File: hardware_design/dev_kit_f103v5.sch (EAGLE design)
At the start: 57 parts, among them J2 CON-SD-CARD_MICROSD-2908-05, U2 FT232RLSSOP, Y1 32.768kHz

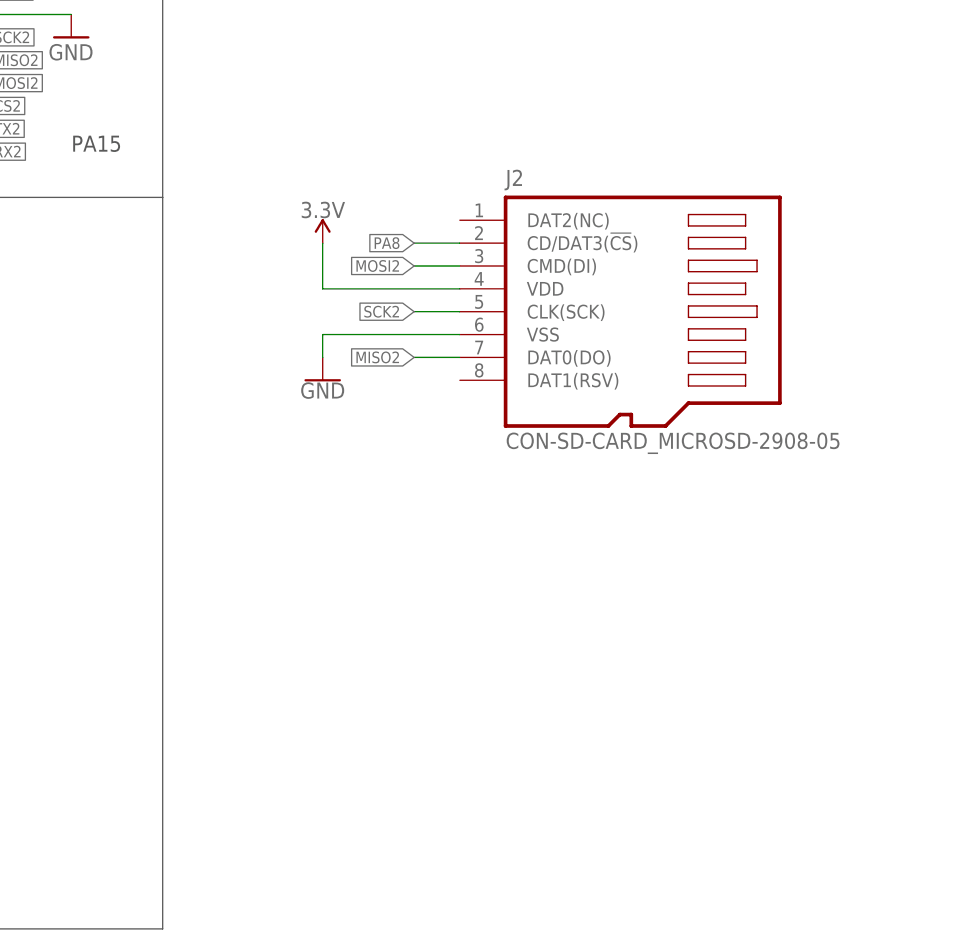
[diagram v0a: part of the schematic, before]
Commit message: Drill size was changed (20 mil)
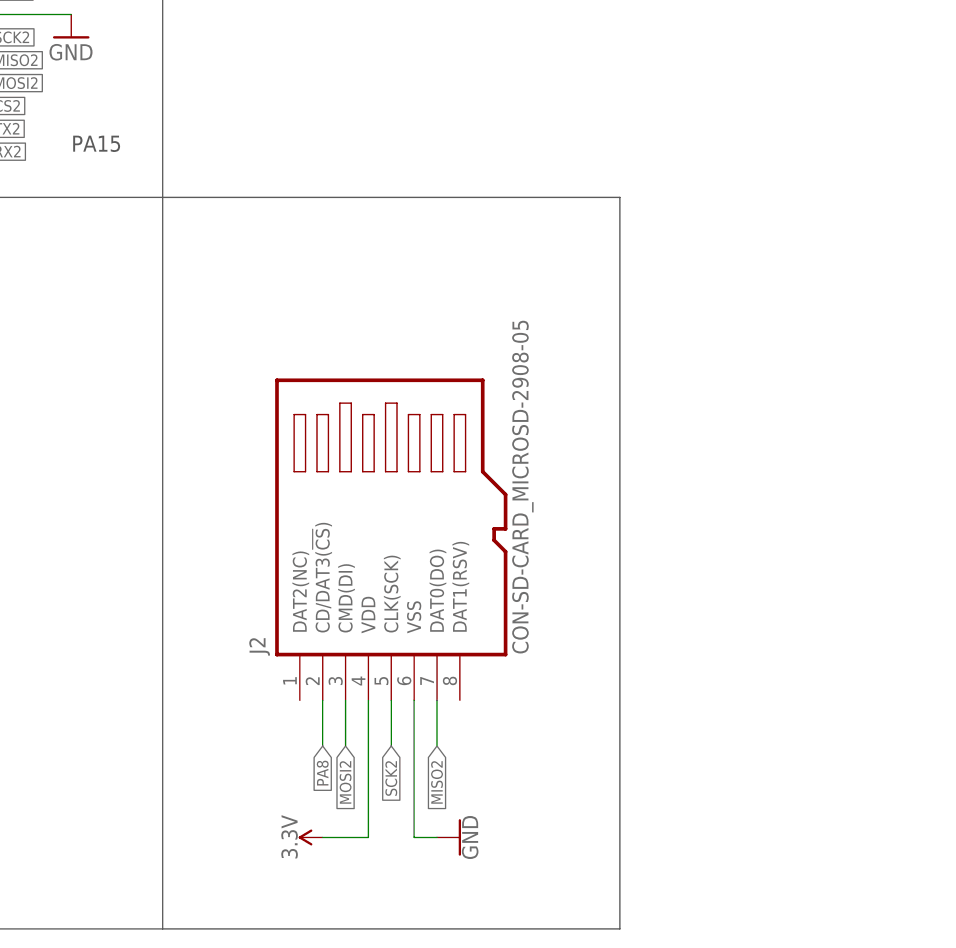
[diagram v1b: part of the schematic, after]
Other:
- moved on the sheet: J2
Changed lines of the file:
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@@
 <text x="139.7" y="139.7" size="1.778" layer="97">PB3</text>
 <text x="7.62" y="15.24" size="1.27" layer="97">CRX3, CTX3, CS2, BUTTON</text>
+<wire x1="180.34" y1="93.98" x2="231.14" y2="93.98" width="0.1524" layer="97"/>
+<wire x1="231.14" y1="93.98" x2="231.14" y2="12.7" width="0.1524" layer="97"/>
+<wire x1="231.14" y1="12.7" x2="180.34" y2="12.7" width="0.1524" layer="97"/>
 </plain>
 <instances>
@@
 <attribute name="VALUE" x="0" y="26.67" size="1.778" layer="96"/>
 </instance>
-<instance part="J2" gate="G$1" x="231.14" y="81.28" smashed="yes">
-<attribute name="NAME" x="218.44" y="95.25" size="1.778" layer="95"/>
-<attribute name="VALUE" x="218.44" y="66.04" size="1.778" layer="96"/>
-</instance>
-<instance part="SUPPLY17" gate="G$1" x="198.12" y="88.9" smashed="yes">
-<attribute name="VALUE" x="198.12" y="91.694" size="1.778" layer="96" align="bottom-center"/>
-</instance>
-<instance part="GND24" gate="1" x="198.12" y="73.66" smashed="yes">
-<attribute name="VALUE" x="198.12" y="73.406" size="1.778" layer="96" align="top-center"/>
+<instance part="J2" gate="G$1" x="205.74" y="55.88" smashed="yes" rot="R90">
+<attribute name="NAME" x="191.77" y="43.18" size="1.778" layer="95" rot="R90"/>
+<attribute name="VALUE" x="220.98" y="43.18" size="1.778" layer="96" rot="R90"/>
+</instance>
+<instance part="SUPPLY17" gate="G$1" x="198.12" y="22.86" smashed="yes" rot="R90">
+<attribute name="VALUE" x="195.326" y="22.86" size="1.778" layer="96" rot="R90" align="bottom-center"/>
+</instance>
+<instance part="GND24" gate="1" x="213.36" y="22.86" smashed="yes" rot="R90">
+<attribute name="VALUE" x="213.614" y="22.86" size="1.778" layer="96" rot="R90" align="top-center"/>
 </instance>
 <instance part="F1" gate="G$1" x="-60.96" y="137.16" smashed="yes">
@@
 <segment>
 <pinref part="J2" gate="G$1" pin="VSS"/>
-<wire x1="213.36" y1="78.74" x2="198.12" y2="78.74" width="0.1524" layer="91"/>
+<wire x1="208.28" y1="38.1" x2="208.28" y2="22.86" width="0.1524" layer="91"/>
 <pinref part="GND24" gate="1" pin="GND"/>
-<wire x1="198.12" y1="78.74" x2="198.12" y2="76.2" width="0.1524" layer="91"/>
+<wire x1="208.28" y1="22.86" x2="210.82" y2="22.86" width="0.1524" layer="91"/>
 </segment>
 </net>
@@
 <segment>
 <pinref part="SUPPLY17" gate="G$1" pin="3.3V"/>
-<wire x1="198.12" y1="88.9" x2="198.12" y2="83.82" width="0.1524" layer="91"/>
+<wire x1="198.12" y1="22.86" x2="203.2" y2="22.86" width="0.1524" layer="91"/>
 <pinref part="J2" gate="G$1" pin="VDD"/>
-<wire x1="198.12" y1="83.82" x2="213.36" y2="83.82" width="0.1524" layer="91"/>
+<wire x1="203.2" y1="22.86" x2="203.2" y2="38.1" width="0.1524" layer="91"/>
 </segment>
 </net>
@@
 <segment>
 <pinref part="J2" gate="G$1" pin="CMD(DI)"/>
-<wire x1="213.36" y1="86.36" x2="208.28" y2="86.36" width="0.1524" layer="91"/>
-<label x="208.28" y="86.36" size="1.27" layer="95" rot="R180" xref="yes"/>
+<wire x1="200.66" y1="38.1" x2="200.66" y2="33.02" width="0.1524" layer="91"/>
+<label x="200.66" y="33.02" size="1.27" layer="95" rot="R270" xref="yes"/>
 </segment>
 </net>
@@
 <segment>
 <pinref part="J2" gate="G$1" pin="DAT0(DO)"/>
-<wire x1="213.36" y1="76.2" x2="208.28" y2="76.2" width="0.1524" layer="91"/>
-<label x="208.28" y="76.2" size="1.27" layer="95" rot="R180" xref="yes"/>
+<wire x1="210.82" y1="38.1" x2="210.82" y2="33.02" width="0.1524" layer="91"/>
+<label x="210.82" y="33.02" size="1.27" layer="95" rot="R270" xref="yes"/>
 </segment>
 </net>
@@
 <segment>
 <pinref part="J2" gate="G$1" pin="CLK(SCK)"/>
-<wire x1="213.36" y1="81.28" x2="208.28" y2="81.28" width="0.1524" layer="91"/>
-<label x="208.28" y="81.28" size="1.27" layer="95" rot="R180" xref="yes"/>
+<wire x1="205.74" y1="38.1" x2="205.74" y2="33.02" width="0.1524" layer="91"/>
+<label x="205.74" y="33.02" size="1.27" layer="95" rot="R270" xref="yes"/>
 </segment>
 </net>
@@
 <segment>
 <pinref part="J2" gate="G$1" pin="CD/DAT3(!CS!)"/>
-<wire x1="213.36" y1="88.9" x2="208.28" y2="88.9" width="0.1524" layer="91"/>
-<label x="208.28" y="88.9" size="1.27" layer="95" rot="R180" xref="yes"/>
-</segment>
-</net>
+<wire x1="198.12" y1="38.1" x2="198.12" y2="33.02" width="0.1524" layer="91"/>
+<label x="198.12" y="33.02" size="1.27" layer="95" rot="R270" xref="yes"/>
+</segment>
+</net>

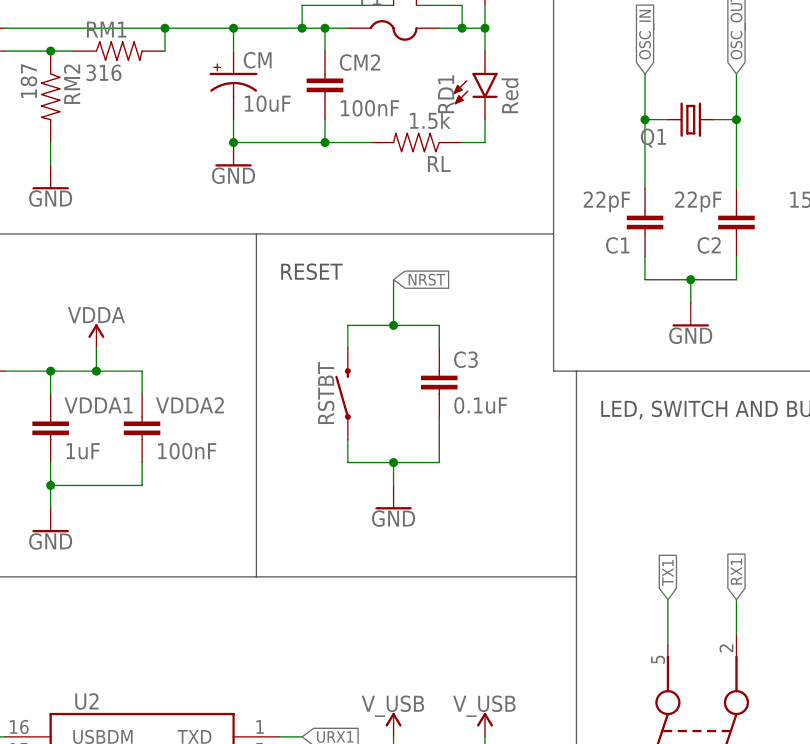
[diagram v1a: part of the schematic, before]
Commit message: Polygon witdh was increased IMPORTANT**
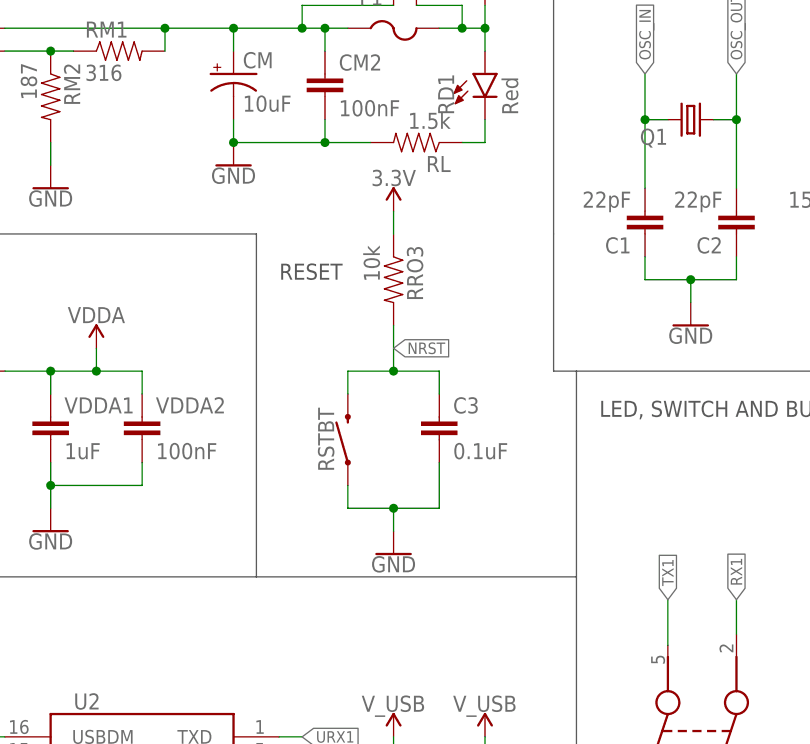
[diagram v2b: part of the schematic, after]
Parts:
- added RRO3: 10k, SparkFun-Resistors:2.0KOHM1/10W5%(0603)
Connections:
- net 3.3V: now also RRO3.1
- net NRST: now also RRO3.2
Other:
- moved on the sheet: C3, RSTBT
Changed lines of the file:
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@@
 <part name="SUPPLY14" library="SparkFun-PowerSymbols" library_urn="urn:adsk.eagle:library:530" deviceset="V_USB" device=""/>
 <part name="SUPPLY18" library="SparkFun-PowerSymbols" library_urn="urn:adsk.eagle:library:530" deviceset="V_USB" device=""/>
+<part name="RRO3" library="SparkFun-Resistors" deviceset="2.0KOHM1/10W5%(0603)" device="" value="10k"/>
+<part name="SUPPLY19" library="SparkFun-PowerSymbols" library_urn="urn:adsk.eagle:library:530" deviceset="3.3V" device=""/>
 </parts>
 <sheets>
@@
 <wire x1="-175.26" y1="149.86" x2="-175.26" y2="116.84" width="0.127" layer="97"/>
 <wire x1="-175.26" y1="116.84" x2="-76.2" y2="116.84" width="0.127" layer="97"/>
-<wire x1="-76.2" y1="116.84" x2="-43.18" y2="116.84" width="0.127" layer="97"/>
 <wire x1="-43.18" y1="116.84" x2="-43.18" y2="149.86" width="0.127" layer="97"/>
 <wire x1="-43.18" y1="149.86" x2="-175.26" y2="149.86" width="0.127" layer="97"/>
@@
 <attribute name="VALUE" x="141.9606" y="57.3786" size="2.0828" layer="96" ratio="6" rot="SR0"/>
 </instance>
-<instance part="RSTBT" gate="G$1" x="-66.04" y="99.06" smashed="yes" rot="R90">
-<attribute name="NAME" x="-67.564" y="99.06" size="1.778" layer="95" font="vector" rot="R90" align="bottom-center"/>
+<instance part="RSTBT" gate="G$1" x="-66.04" y="93.98" smashed="yes" rot="R90">
+<attribute name="NAME" x="-67.564" y="93.98" size="1.778" layer="95" font="vector" rot="R90" align="bottom-center"/>
 </instance>
 <instance part="Q1" gate="G$1" x="-27.94" y="129.54" smashed="yes" rot="R180">
@@
 <attribute name="VALUE" x="-27.94" y="106.426" size="1.778" layer="96" align="top-center"/>
 </instance>
-<instance part="C3" gate="G$1" x="-55.88" y="99.06" smashed="yes">
-<attribute name="NAME" x="-54.356" y="101.981" size="1.778" layer="95" font="vector"/>
-<attribute name="VALUE" x="-54.356" y="96.901" size="1.778" layer="96" font="vector"/>
-</instance>
-<instance part="GND5" gate="1" x="-60.96" y="86.36" smashed="yes">
-<attribute name="VALUE" x="-60.96" y="86.106" size="1.778" layer="96" align="top-center"/>
+<instance part="C3" gate="G$1" x="-55.88" y="93.98" smashed="yes">
+<attribute name="NAME" x="-54.356" y="96.901" size="1.778" layer="95" font="vector"/>
+<attribute name="VALUE" x="-54.356" y="91.821" size="1.778" layer="96" font="vector"/>
+</instance>
+<instance part="GND5" gate="1" x="-60.96" y="81.28" smashed="yes">
+<attribute name="VALUE" x="-60.96" y="81.026" size="1.778" layer="96" align="top-center"/>
 </instance>
 <instance part="C4" gate="G$1" x="-10.16" y="119.38" smashed="yes" rot="R180">
@@
 <instance part="SUPPLY18" gate="G$1" x="-50.8" y="60.96" smashed="yes">
 <attribute name="VALUE" x="-50.8" y="63.754" size="1.778" layer="96" align="bottom-center"/>
+</instance>
+<instance part="RRO3" gate="G$1" x="-60.96" y="111.76" smashed="yes" rot="R270">
+<attribute name="NAME" x="-59.4614" y="115.57" size="1.778" layer="95" rot="R270"/>
+<attribute name="VALUE" x="-64.262" y="115.57" size="1.778" layer="96" rot="R270"/>
+</instance>
+<instance part="SUPPLY19" gate="G$1" x="-60.96" y="119.38" smashed="yes">
+<attribute name="VALUE" x="-60.96" y="122.174" size="1.778" layer="96" align="bottom-center"/>
 </instance>
 </instances>
@@
 <segment>
 <pinref part="RSTBT" gate="G$1" pin="1"/>
-<wire x1="-66.04" y1="93.98" x2="-66.04" y2="91.44" width="0.1524" layer="91"/>
-<wire x1="-66.04" y1="91.44" x2="-60.96" y2="91.44" width="0.1524" layer="91"/>
+<wire x1="-66.04" y1="88.9" x2="-66.04" y2="86.36" width="0.1524" layer="91"/>
+<wire x1="-66.04" y1="86.36" x2="-60.96" y2="86.36" width="0.1524" layer="91"/>
 <pinref part="C3" gate="G$1" pin="2"/>
-<wire x1="-60.96" y1="91.44" x2="-55.88" y2="91.44" width="0.1524" layer="91"/>
-<wire x1="-55.88" y1="91.44" x2="-55.88" y2="96.52" width="0.1524" layer="91"/>
+<wire x1="-60.96" y1="86.36" x2="-55.88" y2="86.36" width="0.1524" layer="91"/>
+<wire x1="-55.88" y1="86.36" x2="-55.88" y2="91.44" width="0.1524" layer="91"/>
 <pinref part="GND5" gate="1" pin="GND"/>
-<wire x1="-60.96" y1="88.9" x2="-60.96" y2="91.44" width="0.1524" layer="91"/>
-<junction x="-60.96" y="91.44"/>
+<wire x1="-60.96" y1="83.82" x2="-60.96" y2="86.36" width="0.1524" layer="91"/>
+<junction x="-60.96" y="86.36"/>
 </segment>
 <segment>
@@
 <wire x1="203.2" y1="22.86" x2="203.2" y2="38.1" width="0.1524" layer="91"/>
 </segment>
+<segment>
+<pinref part="SUPPLY19" gate="G$1" pin="3.3V"/>
+<pinref part="RRO3" gate="G$1" pin="1"/>
+<wire x1="-60.96" y1="119.38" x2="-60.96" y2="116.84" width="0.1524" layer="91"/>
+</segment>
 </net>
 <net name="VIN" class="0">
@@
 <segment>
 <pinref part="RSTBT" gate="G$1" pin="2"/>
-<wire x1="-66.04" y1="104.14" x2="-66.04" y2="106.68" width="0.1524" layer="91"/>
-<wire x1="-66.04" y1="106.68" x2="-60.96" y2="106.68" width="0.1524" layer="91"/>
+<wire x1="-66.04" y1="99.06" x2="-66.04" y2="101.6" width="0.1524" layer="91"/>
 <pinref part="C3" gate="G$1" pin="1"/>
-<wire x1="-60.96" y1="106.68" x2="-55.88" y2="106.68" width="0.1524" layer="91"/>
-<wire x1="-55.88" y1="106.68" x2="-55.88" y2="104.14" width="0.1524" layer="91"/>
-<wire x1="-60.96" y1="106.68" x2="-60.96" y2="111.76" width="0.1524" layer="91"/>
-<junction x="-60.96" y="106.68"/>
-<label x="-60.96" y="111.76" size="1.27" layer="95" xref="yes"/>
-</segment>
-<segment>
+<wire x1="-66.04" y1="101.6" x2="-60.96" y2="101.6" width="0.1524" layer="91"/>
+<wire x1="-60.96" y1="101.6" x2="-55.88" y2="101.6" width="0.1524" layer="91"/>
+<wire x1="-55.88" y1="101.6" x2="-55.88" y2="99.06" width="0.1524" layer="91"/>
+<label x="-60.96" y="104.14" size="1.27" layer="95" xref="yes"/>
+<junction x="-60.96" y="101.6"/>
+<pinref part="RRO3" gate="G$1" pin="2"/>
+<wire x1="-60.96" y1="106.68" x2="-60.96" y2="101.6" width="0.1524" layer="91"/>
+</segment>
+<segment>
